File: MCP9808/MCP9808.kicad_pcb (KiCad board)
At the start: 2 copper layers, 25.4 x 17.8 mm, 25 parts, among them J1 Conn_01x06, J2 Conn_01x04, J3 Conn_01x06, J4 Conn_01x04, U1 MCP9808_MSOP

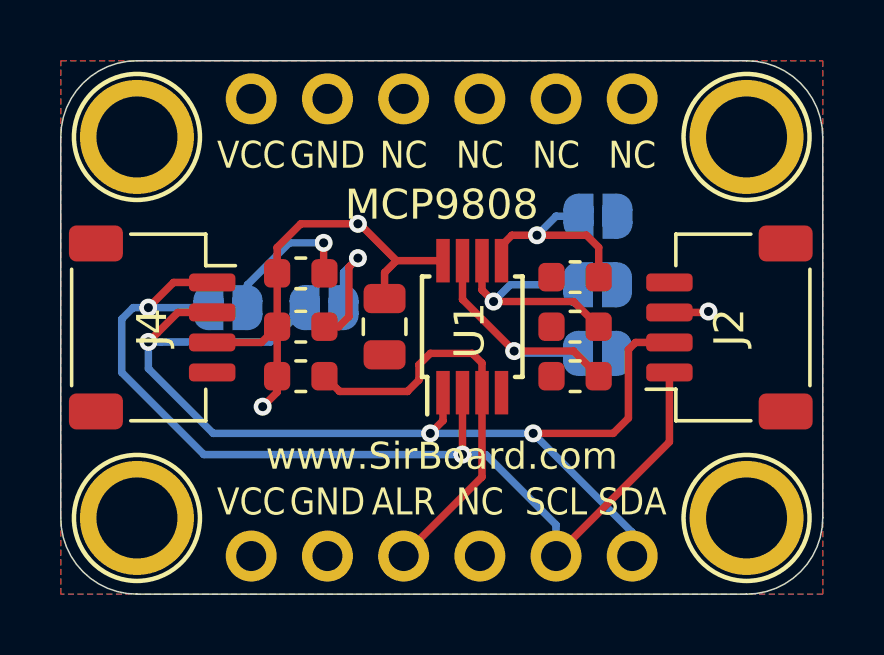
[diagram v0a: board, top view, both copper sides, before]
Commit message: Copper Pour Edits
Copper pour reduced to have 0.2mm edge clearance
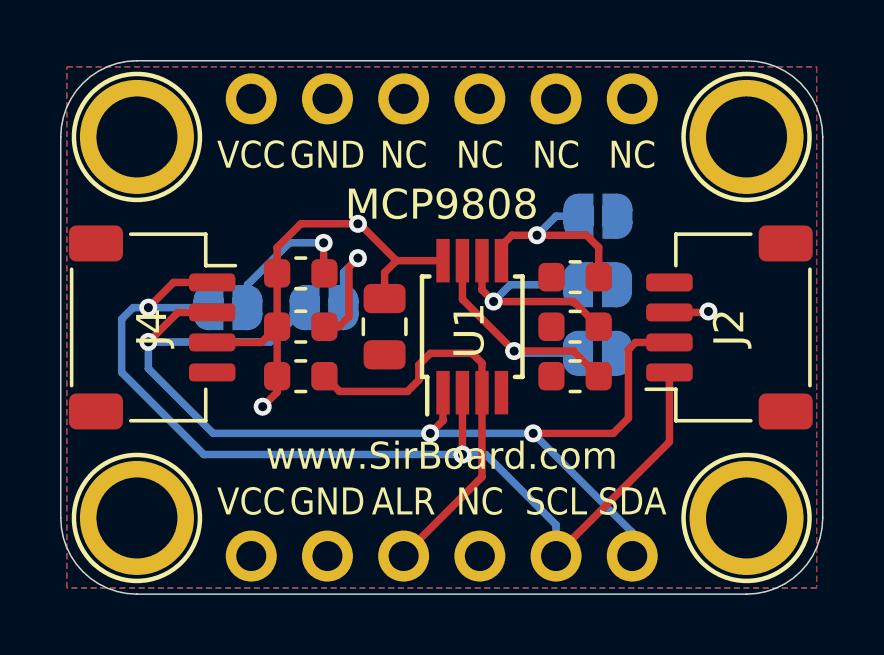
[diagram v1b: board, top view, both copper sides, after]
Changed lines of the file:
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@@
   )
   (setup
-    (last_trace_width 0.25)
+    (last_trace_width 0.127)
     (user_trace_width 0.2)
     (user_trace_width 0.25)
@@
     (polygon
       (pts
-        (xy 52.578 27.0764) (xy 77.978 27.0764) (xy 77.978 44.8564) (xy 52.578 44.8564)
+        (xy 52.7812 27.2796) (xy 77.7748 27.2796) (xy 77.7748 44.6532) (xy 52.7812 44.6532)
       )
     )
@@
     (polygon
       (pts
-        (xy 52.578 27.0764) (xy 77.978 27.0764) (xy 77.978 44.8564) (xy 52.578 44.8564)
+        (xy 52.7812 27.2796) (xy 77.7748 27.2796) (xy 77.7748 44.6532) (xy 52.7812 44.6532)
       )
     )

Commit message: MCP9808 .sch and .pcb update
Address Pins Broken Out
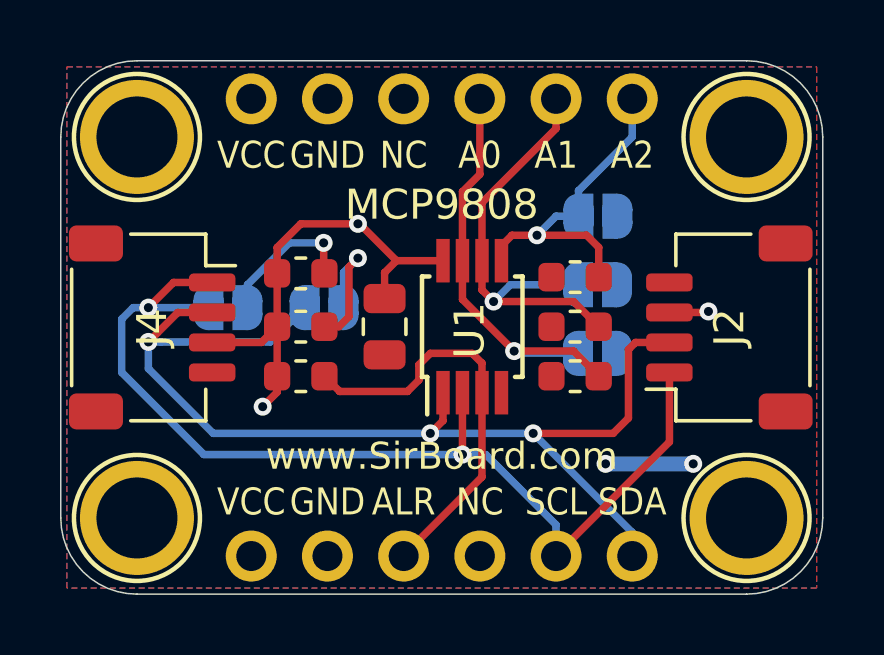
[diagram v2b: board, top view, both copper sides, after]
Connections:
- A0 pad 1: Net-(A0-Pad1) -> A0
- A1 pad 1: Net-(A1-Pad1) -> A1
- A2 pad 1: Net-(A2-Pad1) -> A2
- J3 pad 4: Net-(J3-Pad4) -> A0
- J3 pad 5: Net-(J3-Pad5) -> A1
- J3 pad 6: Net-(J3-Pad6) -> A2
- R3 pad 1: Net-(A2-Pad1) -> A2
- R4 pad 1: Net-(A1-Pad1) -> A1
- R5 pad 1: Net-(A0-Pad1) -> A0
- U1 pad 5: Net-(A2-Pad1) -> A2
- U1 pad 6: Net-(A1-Pad1) -> A1
- U1 pad 7: Net-(A0-Pad1) -> A0
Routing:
- net A1: track 0.00 -> 14.9 mm, vias 0 -> 1
- net A0: track 0.00 -> 14.6 mm, vias 0 -> 1
- net A2: track 0.00 -> 11.4 mm, vias 0 -> 1
- net Net-(A0-Pad1): track 8.96 -> 0.00 mm, vias 1 -> 0
- net Net-(A1-Pad1): track 8.45 -> 0.00 mm, vias 1 -> 0
- net Net-(A2-Pad1): track 6.70 -> 0.00 mm, vias 1 -> 0
- net GND: track 0.00 -> 2.92 mm, vias 0 -> 2
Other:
- board text added: "A0"
- board text added: "A1"
- board text added: "A2"

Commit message: Soldermask width adjusted
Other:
- rule solder_mask_min_width: 0.1 -> 0.05
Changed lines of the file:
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@@
   )
   (setup
-    (last_trace_width 0.5)
+    (last_trace_width 0.127)
     (user_trace_width 0.2)
     (user_trace_width 0.25)
@@
     (pad_drill 1)
     (pad_to_mask_clearance 0)
-    (solder_mask_min_width 0.1)
+    (solder_mask_min_width 0.05)
     (aux_axis_origin 0 0)
     (visible_elements 7FFFFFFF)
@@
   (segment (start 55.499 36.448994) (end 55.499 37.338) (width 0.25) (layer B.Cu) (net 6))
   (segment (start 55.499 37.338) (end 57.658 39.497) (width 0.25) (layer B.Cu) (net 6))
-  (segment (start 65.969 33.741) (end 65.969 35.0318) (width 0.25) (layer F.Cu) (net 10))
-  (segment (start 65.969 35.0318) (end 67.691 36.7538) (width 0.25) (layer F.Cu) (net 10))
-  (segment (start 69.6723 36.7538) (end 70.5105 37.592) (width 0.25) (layer F.Cu) (net 10))
-  (segment (start 67.691 36.7538) (end 69.6723 36.7538) (width 0.25) (layer F.Cu) (net 10))
-  (via (at 67.691 36.7538) (size 0.6) (drill 0.3) (layers F.Cu B.Cu) (net 10))
-  (segment (start 67.75445 36.81725) (end 67.691 36.7538) (width 0.25) (layer B.Cu) (net 10))
-  (segment (start 69.73575 36.81725) (end 67.75445 36.81725) (width 0.25) (layer B.Cu) (net 10))
-  (segment (start 66.619 34.716) (end 67.0058 35.1028) (width 0.25) (layer F.Cu) (net 11))
-  (segment (start 66.619 33.741) (end 66.619 34.716) (width 0.25) (layer F.Cu) (net 11))
-  (segment (start 69.6723 35.1028) (end 70.5105 35.941) (width 0.25) (layer F.Cu) (net 11))
-  (segment (start 67.0058 35.1028) (end 69.6723 35.1028) (width 0.25) (layer F.Cu) (net 11))
-  (via (at 67.0058 35.1028) (size 0.6) (drill 0.3) (layers F.Cu B.Cu) (net 11))
-  (segment (start 67.5646 34.544) (end 67.0058 35.1028) (width 0.25) (layer B.Cu) (net 11))
-  (segment (start 69.85 34.544) (end 67.5646 34.544) (width 0.25) (layer B.Cu) (net 11))
-  (segment (start 67.269 33.241) (end 67.617 32.893) (width 0.25) (layer F.Cu) (net 12))
-  (segment (start 67.269 33.741) (end 67.269 33.241) (width 0.25) (layer F.Cu) (net 12))
-  (segment (start 70.5105 33.2995) (end 70.5105 34.29) (width 0.25) (layer F.Cu) (net 12))
-  (segment (start 70.104 32.893) (end 70.5105 33.2995) (width 0.25) (layer F.Cu) (net 12))
-  (via (at 68.453 32.893) (size 0.6) (drill 0.3) (layers F.Cu B.Cu) (net 12))
-  (segment (start 67.617 32.893) (end 68.453 32.893) (width 0.25) (layer F.Cu) (net 12))
-  (segment (start 68.453 32.893) (end 70.104 32.893) (width 0.25) (layer F.Cu) (net 12))
-  (segment (start 69.088 32.258) (end 68.453 32.893) (width 0.25) (layer B.Cu) (net 12))
-  (segment (start 69.85 32.258) (end 69.088 32.258) (width 0.25) (layer B.Cu) (net 12))
   (segment (start 64.008 43.561) (end 64.008 43.5864) (width 0.25) (layer F.Cu) (net 8))
   (segment (start 66.619 38.141) (end 66.619 40.95) (width 0.25) (layer F.Cu) (net 8))
@@
   (segment (start 66.619 37.155) (end 66.619 38.141) (width 0.25) (layer F.Cu) (net 8))
   (segment (start 66.294 36.83) (end 66.619 37.155) (width 0.25) (layer F.Cu) (net 8))
+  (segment (start 65.969 33.741) (end 65.969 35.0318) (width 0.25) (layer F.Cu) (net 10))
+  (segment (start 65.969 35.0318) (end 67.691 36.7538) (width 0.25) (layer F.Cu) (net 10))
+  (segment (start 69.6723 36.7538) (end 70.5105 37.592) (width 0.25) (layer F.Cu) (net 10))
+  (segment (start 67.691 36.7538) (end 69.6723 36.7538) (width 0.25) (layer F.Cu) (net 10))
+  (via (at 67.691 36.7538) (size 0.6) (drill 0.3) (layers F.Cu B.Cu) (net 10))
+  (segment (start 67.75445 36.81725) (end 67.691 36.7538) (width 0.25) (layer B.Cu) (net 10))
+  (segment (start 69.73575 36.81725) (end 67.75445 36.81725) (width 0.25) (layer B.Cu) (net 10))
   (segment (start 65.969 33.741) (end 65.969 31.44) (width 0.25) (layer F.Cu) (net 10))
   (segment (start 66.548 30.861) (end 66.548 28.3464) (width 0.25) (layer F.Cu) (net 10))
   (segment (start 65.969 31.44) (end 66.548 30.861) (width 0.25) (layer F.Cu) (net 10))
+  (segment (start 66.619 34.716) (end 67.0058 35.1028) (width 0.25) (layer F.Cu) (net 11))
+  (segment (start 66.619 33.741) (end 66.619 34.716) (width 0.25) (layer F.Cu) (net 11))
+  (segment (start 69.6723 35.1028) (end 70.5105 35.941) (width 0.25) (layer F.Cu) (net 11))
+  (segment (start 67.0058 35.1028) (end 69.6723 35.1028) (width 0.25) (layer F.Cu) (net 11))
+  (via (at 67.0058 35.1028) (size 0.6) (drill 0.3) (layers F.Cu B.Cu) (net 11))
+  (segment (start 67.5646 34.544) (end 67.0058 35.1028) (width 0.25) (layer B.Cu) (net 11))
+  (segment (start 69.85 34.544) (end 67.5646 34.544) (width 0.25) (layer B.Cu) (net 11))
   (segment (start 66.619 31.806) (end 66.619 33.741) (width 0.25) (layer F.Cu) (net 11))
   (segment (start 69.088 28.3464) (end 69.088 29.337) (width 0.25) (layer F.Cu) (net 11))
   (segment (start 69.088 29.337) (end 66.619 31.806) (width 0.25) (layer F.Cu) (net 11))
+  (segment (start 67.269 33.241) (end 67.617 32.893) (width 0.25) (layer F.Cu) (net 12))
+  (segment (start 67.269 33.741) (end 67.269 33.241) (width 0.25) (layer F.Cu) (net 12))
+  (segment (start 70.5105 33.2995) (end 70.5105 34.29) (width 0.25) (layer F.Cu) (net 12))
+  (segment (start 70.104 32.893) (end 70.5105 33.2995) (width 0.25) (layer F.Cu) (net 12))
+  (via (at 68.453 32.893) (size 0.6) (drill 0.3) (layers F.Cu B.Cu) (net 12))
+  (segment (start 67.617 32.893) (end 68.453 32.893) (width 0.25) (layer F.Cu) (net 12))
+  (segment (start 68.453 32.893) (end 70.104 32.893) (width 0.25) (layer F.Cu) (net 12))
+  (segment (start 69.088 32.258) (end 68.453 32.893) (width 0.25) (layer B.Cu) (net 12))
+  (segment (start 69.85 32.258) (end 69.088 32.258) (width 0.25) (layer B.Cu) (net 12))
   (segment (start 69.835 31.410408) (end 71.628 29.617408) (width 0.25) (layer B.Cu) (net 12))
   (segment (start 69.835 32.258) (end 69.835 31.410408) (width 0.25) (layer B.Cu) (net 12))
